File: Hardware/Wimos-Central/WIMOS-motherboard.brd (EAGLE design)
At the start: 73 x 71 mm, 7 parts, among them IC2 LD117AS12TR

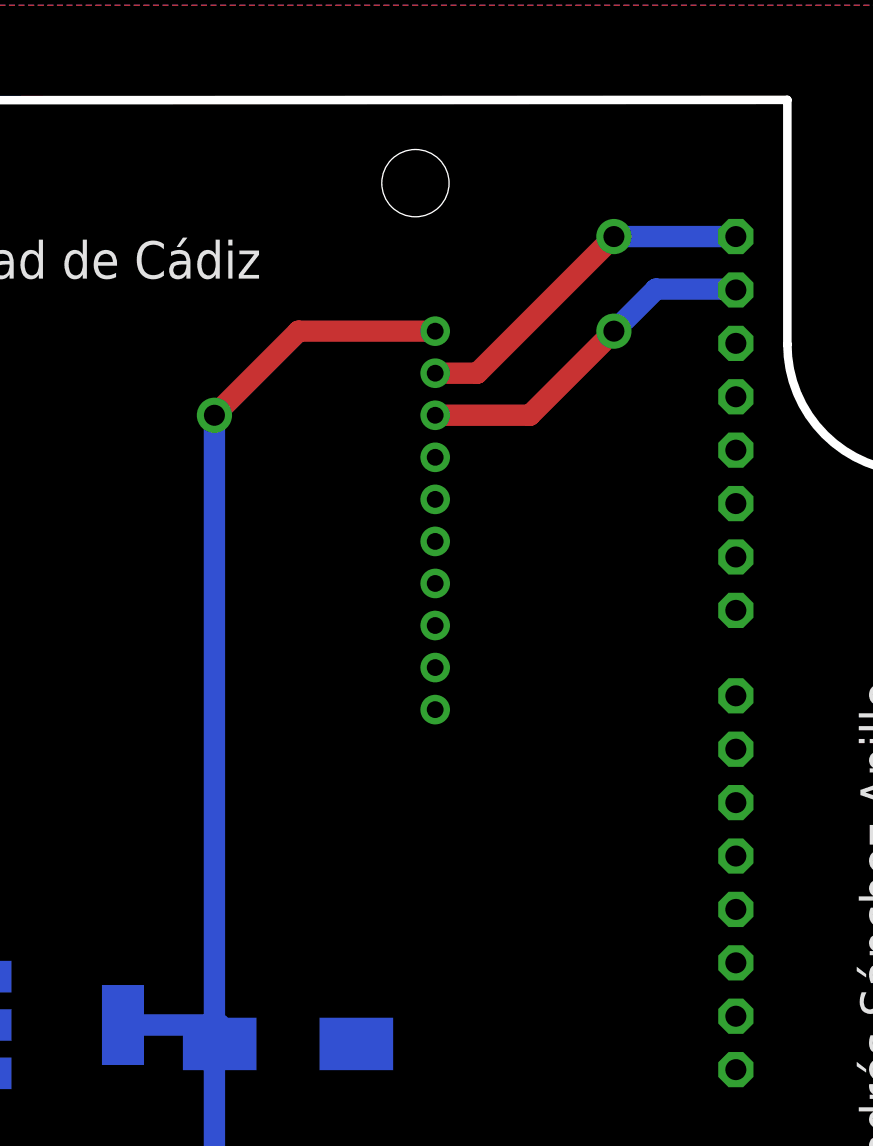
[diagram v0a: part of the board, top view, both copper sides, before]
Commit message: SW
Communication 4bytes packetization.
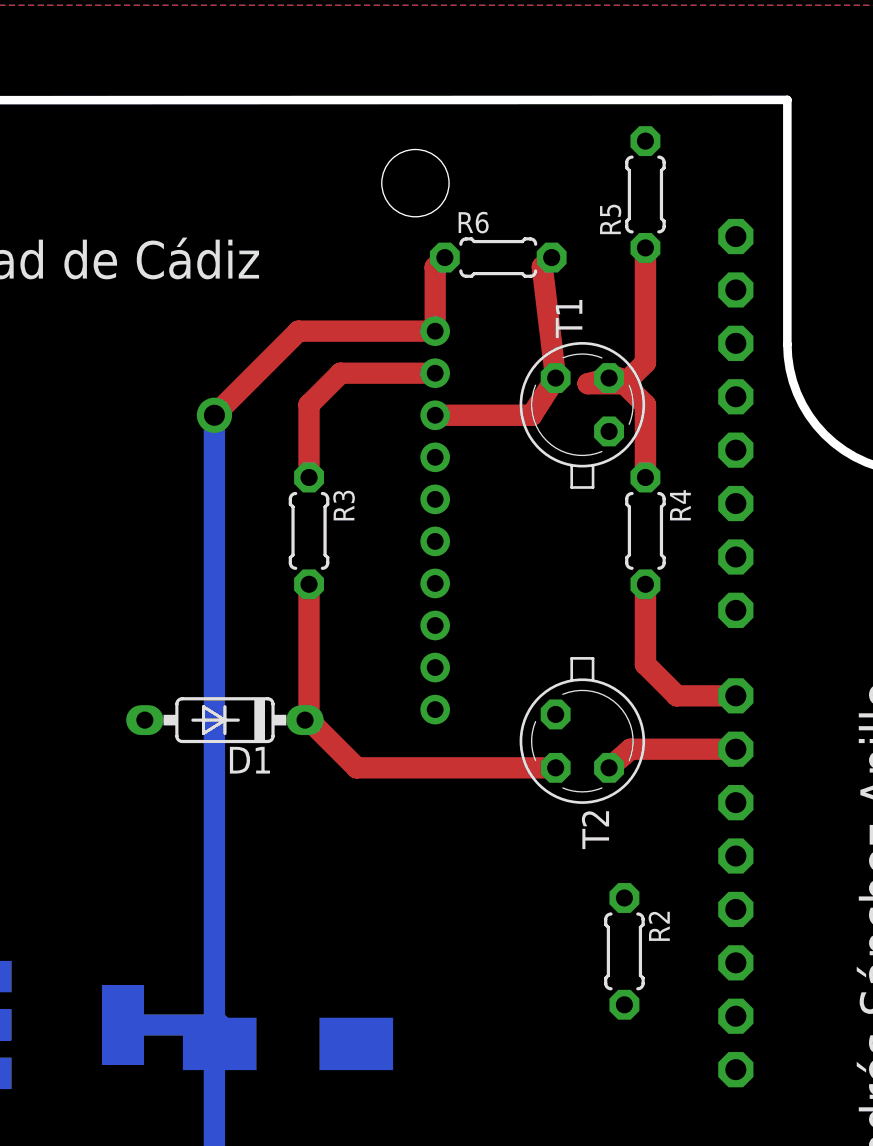
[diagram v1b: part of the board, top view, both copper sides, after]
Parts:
- added D1: 1N4148DO35-7, diode:DO35-7
- added R2, R3, R4, R5, R6: (no value), rcl:0204/5
- added T1, T2: 2N2222, transistor-neu-to92:TO18
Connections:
- new net N$2: D1.C, R3.2, T2.2
- new net N$3: R4.1, R5.1, T1.2
- new net RX_5V: R2.1, T2.3, U$1.D9
- new net TX_5V: R4.2, U$1.D8
- net 3.3V: now also R6.1
- net GND: now also D1.A, R5.2, T1.1, T2.1
- net VCC: now also R2.2
- net XBEE_RX: now also R6.2, T1.3; no longer U$1.D1
- net XBEE_TX: now also R3.1; no longer U$1.D0
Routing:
- net N$2: track 0.00 -> 19.4 mm
- net N$3: track 0.00 -> 15.4 mm
- net TX_5V: track 0.00 -> 8.73 mm
- net XBEE_TX: track 17.0 -> 10.1 mm, vias 1 -> 0
- net RX_5V: track 0.00 -> 6.36 mm
- net XBEE_RX: track 16.8 -> 12.6 mm, vias 1 -> 0
- net 3.3V: track 54.9 -> 58.6 mm
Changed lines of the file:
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@@
 <?xml version="1.0" encoding="utf-8"?>
 <!DOCTYPE eagle SYSTEM "eagle.dtd">
-<eagle version="7.3.0">
+<eagle version="7.7.0">
 <drawing>
 <settings>
@@
 <element name="LED1" library="led" package="LED5MM" value="" x="41.5" y="8" rot="R180"/>
 <element name="R1" library="rcl" package="R0805" value="" x="41.5" y="22.5" rot="MR270"/>
+<element name="T1" library="transistor-neu-to92" package="TO18" value="2N2222" x="59" y="61" rot="R90"/>
+<element name="T2" library="transistor-neu-to92" package="TO18" value="2N2222" x="59" y="45" rot="R270"/>
+<element name="R2" library="rcl" package="0204/5" value="" x="61" y="35" rot="R270"/>
+<element name="R3" library="rcl" package="0204/5" value="" x="46" y="55" rot="R270"/>
+<element name="D1" library="diode" package="DO35-7" value="1N4148DO35-7" x="42" y="46" rot="R180"/>
+<element name="R4" library="rcl" package="0204/5" value="" x="62" y="55" rot="R270"/>
+<element name="R5" library="rcl" package="0204/5" value="" x="62" y="71" rot="R90"/>
+<element name="R6" library="rcl" package="0204/5" value="" x="55" y="68"/>
 </elements>
 <signals>
@@
 <contactref element="C2" pad="2"/>
 <contactref element="LED1" pad="K"/>
+<contactref element="T2" pad="1"/>
+<contactref element="D1" pad="A"/>
+<contactref element="R5" pad="2"/>
+<contactref element="T1" pad="1"/>
 </signal>
 <signal name="VIN">
 <contactref element="U$1" pad="VIN"/>
 </signal>
-<signal name="3V">
-<contactref element="U$1" pad="3V"/>
-</signal>
 <signal name="XBEE_TX">
 <contactref element="ZIGBEE_MODULE" pad="2"/>
-<contactref element="U$1" pad="D0"/>
-<wire x1="66.3" y1="69" x2="60.5" y2="69" width="1.016" layer="16"/>
-<via x="60.5" y="69" extent="1-16" drill="1" diameter="1.6764"/>
-<wire x1="60.5" y1="69" x2="54" y2="62.5" width="1.016" layer="1"/>
-<wire x1="54" y1="62.5" x2="52" y2="62.5" width="1.016" layer="1"/>
+<contactref element="R3" pad="1"/>
+<wire x1="52" y1="62.5" x2="47.5" y2="62.5" width="1.016" layer="1"/>
+<wire x1="47.5" y1="62.5" x2="46" y2="61" width="1.016" layer="1"/>
+<wire x1="46" y1="61" x2="46" y2="57.54" width="1.016" layer="1"/>
 </signal>
 <signal name="XBEE_RX">
 <contactref element="ZIGBEE_MODULE" pad="3"/>
-<contactref element="U$1" pad="D1"/>
-<wire x1="66.3" y1="66.46" x2="66.26" y2="66.5" width="1.016" layer="16"/>
-<wire x1="66.26" y1="66.5" x2="62.5" y2="66.5" width="1.016" layer="16"/>
-<wire x1="62.5" y1="66.5" x2="60.5" y2="64.5" width="1.016" layer="16"/>
-<via x="60.5" y="64.5" extent="1-16" drill="1" diameter="1.6764"/>
-<wire x1="60.5" y1="64.5" x2="56.5" y2="60.5" width="1.016" layer="1"/>
-<wire x1="56.5" y1="60.5" x2="52" y2="60.5" width="1.016" layer="1"/>
+<contactref element="T1" pad="3"/>
+<contactref element="R6" pad="2"/>
+<wire x1="57.54" y1="68" x2="57.095" y2="67.555" width="1.016" layer="1"/>
+<wire x1="57.095" y1="67.555" x2="57.73" y2="62.27" width="1.016" layer="1"/>
+<wire x1="52" y1="60.5" x2="56.595" y2="60.5" width="1.016" layer="1"/>
+<wire x1="56.595" y1="60.5" x2="57.73" y2="62.27" width="1.016" layer="1"/>
 </signal>
 <signal name="XBEE_ON">
@@
 <wire x1="28" y1="34" x2="28.2" y2="33.8" width="1.016" layer="16"/>
 <wire x1="28.2" y1="33.8" x2="30.85" y2="33.8" width="1.016" layer="16"/>
+<contactref element="R2" pad="2"/>
+<wire x1="30.85" y1="33.8" x2="61" y2="32.46" width="0" layer="19" extent="16-16"/>
 </signal>
 <signal name="3.3V">
@@
 <wire x1="41.75" y1="30.6" x2="41.675" y2="30.6" width="0.4064" layer="16"/>
 <wire x1="41.675" y1="30.6" x2="41.675" y2="31.425" width="0.4064" layer="16"/>
+<contactref element="R6" pad="1"/>
+<wire x1="52.46" y1="68" x2="52" y2="67.54" width="1.016" layer="1"/>
+<wire x1="52" y1="67.54" x2="52" y2="64.5" width="1.016" layer="1"/>
 </signal>
 <signal name="N$1">
@@
 <wire x1="42.77" y1="14.23" x2="42.77" y2="8" width="1.016" layer="16"/>
 </signal>
+<signal name="RX_5V">
+<contactref element="U$1" pad="D9"/>
+<contactref element="T2" pad="3"/>
+<contactref element="R2" pad="1"/>
+<wire x1="60.27" y1="43.73" x2="61.289" y2="44.616" width="1.016" layer="1"/>
+<wire x1="61.289" y1="44.616" x2="66.3" y2="44.616" width="1.016" layer="1"/>
+<wire x1="61" y1="37.54" x2="61.289" y2="44.616" width="0" layer="19" extent="1-1"/>
+</signal>
+<signal name="TX_5V">
+<contactref element="U$1" pad="D8"/>
+<contactref element="R4" pad="2"/>
+<wire x1="63.494" y1="47.156" x2="66.3" y2="47.156" width="1.016" layer="1"/>
+<wire x1="62" y1="52.46" x2="62" y2="48.65" width="1.016" layer="1"/>
+<wire x1="62" y1="48.65" x2="63.494" y2="47.156" width="1.016" layer="1"/>
+</signal>
+<signal name="3V">
+<contactref element="U$1" pad="3V"/>
+</signal>
+<signal name="N$2">
+<contactref element="T2" pad="2"/>
+<contactref element="R3" pad="2"/>
+<contactref element="D1" pad="C"/>
+<wire x1="46" y1="52.46" x2="46" y2="46.19" width="1.016" layer="1"/>
+<wire x1="46" y1="46.19" x2="45.81" y2="46" width="1.016" layer="1"/>
+<wire x1="46" y1="46.19" x2="46" y2="46" width="1.016" layer="1"/>
+<wire x1="46" y1="46" x2="48.27" y2="43.73" width="1.016" layer="1"/>
+<wire x1="48.27" y1="43.73" x2="57.73" y2="43.73" width="1.016" layer="1"/>
+</signal>
+<signal name="N$3">
+<contactref element="R4" pad="1"/>
+<contactref element="R5" pad="1"/>
+<contactref element="T1" pad="2"/>
+<wire x1="62" y1="68.46" x2="62" y2="63" width="1.016" layer="1"/>
+<wire x1="62" y1="63" x2="61" y2="62" width="1.016" layer="1"/>
+<wire x1="61" y1="62" x2="59.27" y2="62" width="1.016" layer="1"/>
+<wire x1="59.27" y1="62" x2="60.27" y2="62.27" width="1.016" layer="1"/>
+<wire x1="62" y1="57.54" x2="62" y2="61" width="1.016" layer="1"/>
+<wire x1="62" y1="61" x2="60.73" y2="62.27" width="1.016" layer="1"/>
+<wire x1="60.73" y1="62.27" x2="60.27" y2="62.27" width="1.016" layer="1"/>
+</signal>
 </signals>

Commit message: DOC + HW
Doc incremento 1 y 2 (Implementación)
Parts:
- removed D1: 1N4148DO35-7, diode:DO35-7
- removed R2, R3, R4, R5, R6: (no value), rcl:0204/5
- removed T1, T2: 2N2222, transistor-neu-to92:TO18
- added R10, R7, R8: 2.2k, rcl:0204/5
- added R9: 1k, rcl:0204/5
- added T3: KSP2222A, transistor:TO92-CBE
- R1: value (none) -> 2.2k
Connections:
- net 3V renamed 3V3
- removed net N$2: D1.C, R3.2, T2.2
- removed net N$3: R4.1, R5.1, T1.2
- new net N$4: R8.2, T3.B
- net 3.3V: now also R8.1; no longer R6.1
- net GND: now also R10.2; no longer D1.A, R5.2, T1.1, T2.1
- net RX_5V: now also R7.2, T3.C, U$1.D8; no longer R2.1, T2.3, U$1.D9
- net TX_5V: now also R9.1, U$1.D9; no longer R4.2, U$1.D8
- net VCC: now also R7.1; no longer R2.2
- net XBEE_RX: now also R10.1, R9.2; no longer R6.2, T1.3
- net XBEE_TX: now also T3.E; no longer R3.1
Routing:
- net RX_5V: track 6.36 -> 26.3 mm
- net N$2: track 19.4 -> 0.00 mm
- net N$3: track 15.4 -> 0.00 mm
- net VCC: track 20.1 -> 33.8 mm
- net XBEE_TX: track 10.1 -> 17.2 mm
- net XBEE_RX: track 12.6 -> 19.5 mm
- net N$4: track 0.00 -> 4.46 mm
- net TX_5V: track 8.73 -> 4.36 mm
- net 3.3V: track 58.6 -> 60.2 mm
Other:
- board text removed: "Escala 1.5 : 1"
